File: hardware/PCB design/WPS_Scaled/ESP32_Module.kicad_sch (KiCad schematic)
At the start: 0 parts

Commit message: finalized the pcb schematics
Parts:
- added C20, C7: 100nF, symbol Device:C
- added C21, C23: 0.1uF, symbol Device:C
- added C22: 10uF, symbol Device:C_Polarized
- added C6: 22uF, symbol Device:C_Polarized
- added C8, C9: 1uF, symbol Device:C
- added D12, D13, D14, D4: LED, symbol Device:LED
- added D3: 1N5817-T, 1N5817-T:DIOAD1039W78L463D236, symbol COIL_1N5817-T:1N5817-T
- added R26, R27: 2.2k, symbol Device:R
- added R28, R5, R6: 10k, symbol Device:R
- added R3, R4: 5.1k, symbol Device:R
- added R7: 1k, symbol Device:R
- added S1, S2: SW_Push, symbol Switch:SW_Push
- added TP_BOOT1, TP_EN1, TP_RXD0, TP_SCL1, TP_SDA1, TP_TXD0: TestPoint, symbol Connector:TestPoint
- added U3: ESP32-S3-WROOM-1(N16R8), :WIRELM-SMD_ESP32-S3-WROOM-1, symbol COIL:ESP32-S3-WROOM-1(N16R8)
- added U4: TYPEC-306DDW-ARP16, :USB-C-TH_TYPEC-306DDW-ARP16, symbol COIL:TYPEC-306DDW-ARP16
- added U5: CH340C, :SOP-16_L10.0-W3.9-P1.27-LS6.0-BL, symbol COIL:CH340C
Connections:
- new net: D3.2, U4.16 (VBUS), U4.21 (VBUS), U4.4 (VBUS), U4.9 (VBUS)
- new net: D12.2 (A), R26.2
- new net: R3.2, U4.8 (CC1)
- new net: C21.1, U5.4 (V3)
- new net: D4.2 (A), R7.2
- new net: D14.2 (A), R28.2
- new net: R4.1, U4.20 (CC2)
- new net: D13.2 (A), R27.2
- new net: C22.2, C23.2, U5.16 (VCC)
- new net +12V: R28.1
- new net +3.3V: C6.1, C7.1, R5.1, R6.1, R7.1, U3.2 (3V3)
- new net +5V: C22.1, C23.1, D3.1, R26.1
- new net +5V_SW: R27.1
- new net ACTUATOR_PUMP_EN: U3.8 (IO15)
- new net ACTUATOR_UV_EN: U3.9 (IO16)
- new net ACTUATOR_VALVE_EN: U3.10 (IO17)
- new net BUTTON_BOOT: C9.2, R6.2, S2.2, TP_BOOT1.1, U3.27 (IO0)
- new net BUTTON_EN: C20.1, C8.2, R5.2, S1.2, TP_EN1.1, U3.3 (EN)
- new net BUTTON_SYSTEM_RESET: U3.23 (IO21)
- new net DISPLAY_SCL: U3.22 (IO14)
- new net DISPLAY_SDA: U3.21 (IO13)
- new net GND: C20.2, C21.2, C6.2, C7.2, C8.1, C9.1, D12.1 (K), D13.1 (K), D14.1 (K), D4.1 (K), R3.1, R4.2, S1.1, S2.1, U3.1 (GND), U3.40 (GND), U3.41 (GND), U4.1 (GND), U4.12 (GND), U4.13 (GND), U4.17 (SBU2), U4.18 (DN2), U4.19 (DP2), U4.20 (CC2), U4.24 (GND), U5.1 (GND)
- new net LED_MAINTENANCE: U3.12 (IO8)
- new net LED_POWER_ON: U3.11 (IO18)
- new net SENSOR_COLOR_SCL: TP_SCL1.1, U3.24 (IO47)
- new net SENSOR_COLOR_SDA: TP_SDA1.1, U3.25 (IO48)
- new net SENSOR_FLOW_SIGNAL: U3.39 (IO1)
- new net SENSOR_LEVEL_ECHO: U3.35 (IO42)
- new net SENSOR_LEVEL_TRIG: U3.38 (IO2)
- new net SENSOR_PH_SIGNAL: U3.5 (IO5)
- new net SENSOR_PRESSURE_SIGNAL: U3.7 (IO7)
- new net SENSOR_TDS_SIGNAL: U3.6 (IO6)
- new net SENSOR_TURBIDITY_SIGNAL: U3.4 (IO4)
- new net SWITCHED_5V_EN: U3.18 (IO10)
- new net UART_RX: TP_TXD0.1, U3.37 (TXD0), U5.3 (RXD)
- new net UART_TX: TP_RXD0.1, U3.36 (RXD0), U5.2 (TXD)
- new net USB_D+: U4.19 (DP2), U4.7 (DP1), U5.5 (D+)
- new net USB_D-: U4.18 (DN2), U4.6 (DN1), U5.6 (D-)
- no-connect marks 0 -> 26
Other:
- note added: "Caution: Limit total USB current draw to <500mA. Excessive peripheral (sensor) load may trigger host port overcurrent protection, requiring a system restart to reset the port."
- note added: "D4 - Led used to show 3.3V is supplied D12- Led used to show 5V is supplied D13 - Led used to show 5V_SW (required by sensors) is supplied D14 - Led used to show 12V is supplied"
- note added: "EN and BOOT Buttons"
- note added: "ESP32-S3-WROOM-1 module"
- note added: "Power Status Indicators"
- note added: "USB (TYPE-C) module"
- company: (none) -> Makerere University

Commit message: finallized pcb layout
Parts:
- added R30, R31, R32, R33: 4.7k, COIL:RES-TH_BD2.4-L6.3-P10.30-D0.6, symbol Device:R
- C20, C21, C23, C7: footprint (none) -> COIL:CAP-TH_L3.6-W2.3-P2.50-D0.5
- C22: footprint (none) -> COIL:CAP-TH_BD4.0-P2.50-D0.6-FD
- C6: footprint (none) -> COIL:CAP-TH_BD4.8-P2.54-D0.5-RD
- C8, C9: footprint (none) -> COIL:CAP-TH_L4.4-W4.0-P5.08-D0.6
- D3: footprint 1N5817-T:DIOAD1039W78L463D236 -> COIL:DO-27_BD5.2-L8.9-P12.90-D1.5-RD
- LED1: renamed from D4; footprint (none) -> COIL:LED-TH_BD5.9-P2.54-RD_RED
- LED2: renamed from D12; footprint (none) -> COIL:LED-TH_BD5.9-P2.54-RD_RED
- LED3: renamed from D13; footprint (none) -> COIL:LED-TH_BD5.9-P2.54-RD_RED
- LED4: renamed from D14; footprint (none) -> COIL:LED-TH_BD5.9-P2.54-RD_RED
- R26, R27, R28, R3, R4, R5, R6, R7: footprint (none) -> COIL:RES-TH_BD2.4-L6.3-P10.30-D0.6
- S1, S2: footprint (none) -> COIL:KEY-SMD_4P-L6.0-W6.0-P3.90-LS9.0
- TP10: renamed from TP_SDA1; value TestPoint -> SDA1; footprint (none) -> TestPoint:TestPoint_THTPad_D2.0mm_Drill1.0mm
- TP11: renamed from TP_SCL1; value TestPoint -> SCL1; footprint (none) -> TestPoint:TestPoint_THTPad_D2.0mm_Drill1.0mm
- TP6: renamed from TP_EN1; value TestPoint -> EN; footprint (none) -> TestPoint:TestPoint_THTPad_D2.0mm_Drill1.0mm
- TP7: renamed from TP_TXD0; value TestPoint -> TXD0; footprint (none) -> TestPoint:TestPoint_THTPad_D2.0mm_Drill1.0mm
- TP8: renamed from TP_RXD0; value TestPoint -> RXD0; footprint (none) -> TestPoint:TestPoint_THTPad_D2.0mm_Drill1.0mm
- TP9: renamed from TP_BOOT1; value TestPoint -> BOOT; footprint (none) -> TestPoint:TestPoint_THTPad_D2.0mm_Drill1.0mm
- U3: footprint :WIRELM-SMD_ESP32-S3-WROOM-1 -> COIL:WIRELM-SMD_ESP32-S3-WROOM-1
- U4: footprint :USB-C-TH_TYPEC-306DDW-ARP16 -> COIL:USB-C-TH_TYPEC-306DDW-ARP16
- U5: footprint :SOP-16_L10.0-W3.9-P1.27-LS6.0-BL -> COIL:SOP-16_L10.0-W3.9-P1.27-LS6.0-BL
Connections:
- net BUTTON_BOOT: now also C9.1, S2.1; no longer C9.2, S2.2
- net BUTTON_EN: now also C8.1, S1.1; no longer C8.2, S1.2
- net DISPLAY_SCL: now also R31.1
- net DISPLAY_SDA: now also R30.1
- net GND: now also C8.2, C9.2, S1.2, S2.2, U4.A1 (GND), U4.A12 (GND), U4.B1 (GND), U4.B12 (GND); no longer C8.1, C9.1, S1.1, S2.1, U4.1 (GND), U4.12 (GND), U4.13 (GND), U4.24 (GND)
- net SENSOR_COLOR_SCL: now also R33.2
- net SENSOR_COLOR_SDA: now also R32.1
- net LED2_P: now reaches LED2.2 (A), R26.2
- net USB_CC1: now reaches R3.2
- net USB_CC1: now also U4.A5 (CC1); no longer U4.8 (CC1)
- net USB_TO_UART_V3: now reaches C21.1, U5.4 (V3)
- net LED1_P: now reaches LED1.2 (A), R7.2
- net LED4_P: now reaches LED4.2 (A), R28.2
- net USB_CC2: now reaches R4.1
- net USB_CC2: now also U4.B5 (CC2); no longer U4.20 (CC2)
- net LED3_P: now reaches LED3.2 (A), R27.2
- net USB_TO_UART_VCC: now reaches C22.2, C23.2, U5.16 (VCC)
- net +12V renamed VBAT
- net +3.3V renamed +3V3
- net +3V3: now also R30.2, R31.2, R32.2, R33.1
- removed net USB_D+: U4.19 (DP2), U4.7 (DP1), U5.5 (D+)
- removed net USB_D-: U4.18 (DN2), U4.6 (DN1), U5.6 (D-)
- new net USB_DN: U4.A7 (DN1), U4.B7 (DN2), U5.6 (D-)
- new net USB_DP: U4.A6 (DP1), U4.B6 (DP2), U5.5 (D+)
- new net USB_VBUS: D3.2, U4.A4 (VBUS), U4.A9 (VBUS), U4.B4 (VBUS), U4.B9 (VBUS)
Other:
- note added: "Review: It is recommended to connect a 499 Ω series resistor to the U0TXD line to suppress harmonics.(TX line) Make power taces as thick as possible: Main 3.3V line ≥ 25 mil RF power pins (pin2 & pin3) ≥ 20 mil Other small power branches ≥ 10 mil"
- moved on the sheet: C20, C22, C23, C6, C7, C8, C9, LED1, LED2, LED3, LED4, R26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

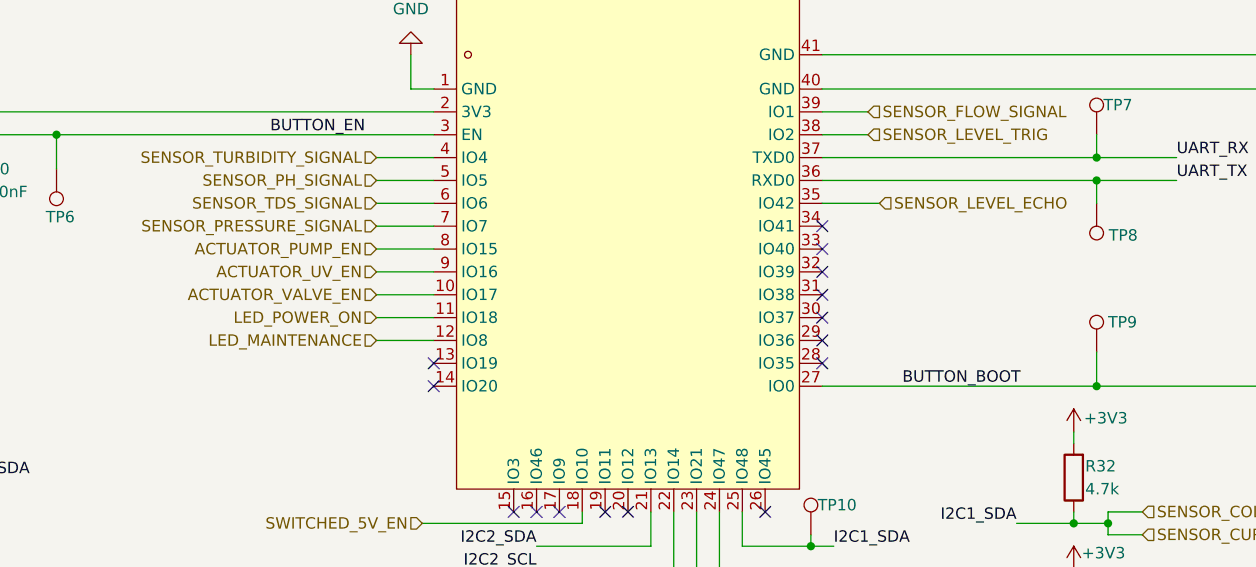
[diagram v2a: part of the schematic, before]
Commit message: started routing with sensors and critical signals
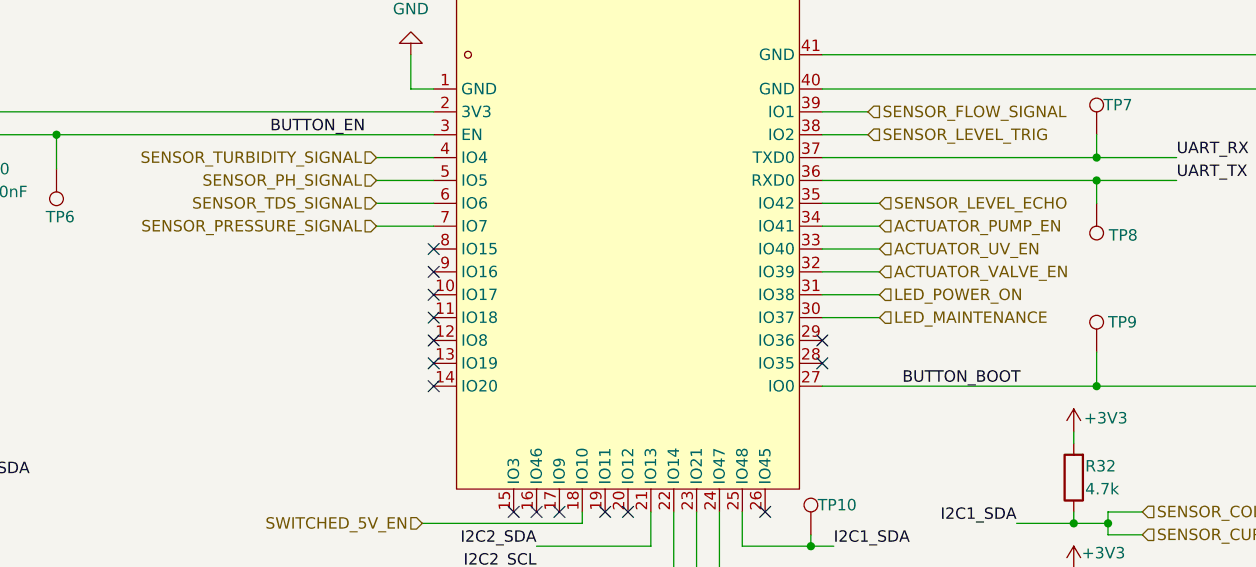
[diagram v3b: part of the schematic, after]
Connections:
- net ACTUATOR_PUMP_EN: now also U3.34 (IO41); no longer U3.8 (IO15)
- net ACTUATOR_UV_EN: now also U3.33 (IO40); no longer U3.9 (IO16)
- net ACTUATOR_VALVE_EN: now also U3.32 (IO39); no longer U3.10 (IO17)
- net LED_MAINTENANCE: now also U3.30 (IO37); no longer U3.12 (IO8)
- net LED_POWER_ON: now also U3.31 (IO38); no longer U3.11 (IO18)
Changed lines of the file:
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@@
-	)
-	(no_connect
-		(at 144.78 67.31)
-	)
-	(no_connect
-		(at 144.78 59.69)
 	)
 	(no_connect
@@
 	)
 	(no_connect
-		(at 144.78 62.23)
+		(at 101.6 69.85)
 	)
 	(no_connect
@@
 	)
 	(no_connect
+		(at 101.6 64.77)
+	)
+	(no_connect
 		(at 138.43 91.44)
 	)
@@
 	)
 	(no_connect
-		(at 144.78 69.85)
-	)
-	(no_connect
 		(at 44.45 157.48)
 	)
@@
 	)
 	(no_connect
+		(at 101.6 72.39)
+	)
+	(no_connect
 		(at 144.78 151.13)
 	)
 	(no_connect
+		(at 101.6 62.23)
+	)
+	(no_connect
 		(at 144.78 74.93)
 	)
@@
 	)
 	(no_connect
-		(at 144.78 64.77)
+		(at 101.6 67.31)
 	)
 	(wire
@@
 	(wire
 		(pts
+			(xy 144.78 69.85) (xy 151.13 69.85)
+		)
+		(stroke
+			(width 0)
+			(type default)
+		)
+	)
+	(wire
+		(pts
 			(xy 71.12 186.69) (xy 71.12 175.26)
 		)
@@
 	(wire
 		(pts
-			(xy 95.25 67.31) (xy 101.6 67.31)
-		)
-		(stroke
-			(width 0)
-			(type default)
-		)
-	)
-	(wire
-		(pts
 			(xy 115.57 151.13) (xy 121.92 151.13)
 		)
@@
 	(wire
 		(pts
-			(xy 95.25 72.39) (xy 101.6 72.39)
-		)
-		(stroke
-			(width 0)
-			(type default)
-		)
-	)
-	(wire
-		(pts
 			(xy 96.52 138.43) (xy 96.52 139.7)
 		)
@@
 	(wire
 		(pts
-			(xy 95.25 69.85) (xy 101.6 69.85)
-		)
-		(stroke
-			(width 0)
-			(type default)
-		)
-	)
-	(wire
-		(pts
 			(xy 57.15 134.62) (xy 22.86 134.62)
 		)
@@
 	(wire
 		(pts
+			(xy 144.78 59.69) (xy 151.13 59.69)
+		)
+		(stroke
+			(width 0)
+			(type default)
+		)
+	)
+	(wire
+		(pts
 			(xy 54.61 138.43) (xy 59.69 138.43)
 		)
@@
 	(wire
 		(pts
-			(xy 95.25 62.23) (xy 101.6 62.23)
-		)
-		(stroke
-			(width 0)
-			(type default)
-		)
-	)
-	(wire
-		(pts
 			(xy 135.89 95.25) (xy 143.51 95.25)
 		)
@@
 	(wire
 		(pts
+			(xy 144.78 67.31) (xy 151.13 67.31)
+		)
+		(stroke
+			(width 0)
+			(type default)
+		)
+	)
+	(wire
+		(pts
 			(xy 35.56 46.99) (xy 101.6 46.99)
 		)
@@
 	(wire
 		(pts
-			(xy 95.25 64.77) (xy 101.6 64.77)
-		)
-		(stroke
-			(width 0)
-			(type default)
-		)
-	)
-	(wire
-		(pts
 			(xy 257.81 66.04) (xy 261.62 66.04)
 		)
@@
 	(wire
 		(pts
+			(xy 144.78 64.77) (xy 151.13 64.77)
+		)
+		(stroke
+			(width 0)
+			(type default)
+		)
+	)
+	(wire
+		(pts
 			(xy 91.44 167.64) (xy 91.44 154.94)
 		)
@@
 		(pts
 			(xy 77.47 146.05) (xy 77.47 138.43)
+		)
+		(stroke
+			(width 0)
+			(type default)
+		)
+	)
+	(wire
+		(pts
+			(xy 144.78 62.23) (xy 151.13 62.23)
 		)
 		(stroke
@@
 	(hierarchical_label "ACTUATOR_UV_EN"
 		(shape input)
-		(at 95.25 64.77 180)
-		(effects
-			(font
-				(size 1.27 1.27)
-			)
-			(justify right)
+		(at 151.13 62.23 0)
+		(effects
+			(font
+				(size 1.27 1.27)
+			)
+			(justify left)
 		)
 	)
@@
 	(hierarchical_label "ACTUATOR_PUMP_EN"
 		(shape input)
-		(at 95.25 62.23 180)
-		(effects
-			(font
-				(size 1.27 1.27)
-			)
-			(justify right)
+		(at 151.13 59.69 0)
+		(effects
+			(font
+				(size 1.27 1.27)
+			)
+			(justify left)
 		)
 	)
@@
 	(hierarchical_label "ACTUATOR_VALVE_EN"
 		(shape input)
-		(at 95.25 67.31 180)
-		(effects
-			(font
-				(size 1.27 1.27)
-			)
-			(justify right)
+		(at 151.13 64.77 0)
+		(effects
+			(font
+				(size 1.27 1.27)
+			)
+			(justify left)
 		)
 	)
@@
 	(hierarchical_label "LED_POWER_ON"
 		(shape input)
-		(at 95.25 69.85 180)
-		(effects
-			(font
-				(size 1.27 1.27)
-			)
-			(justify right)
+		(at 151.13 67.31 0)
+		(effects
+			(font
+				(size 1.27 1.27)
+			)
+			(justify left)
 		)
 	)
@@
 	(hierarchical_label "LED_MAINTENANCE"
 		(shape input)
-		(at 95.25 72.39 180)
-		(effects
-			(font
-				(size 1.27 1.27)
-			)
-			(justify right)
-		)
-	)
+		(at 151.13 69.85 0)
+		(effects
+			(font
+				(size 1.27 1.27)
+			)
+			(justify left)
+		)
+	)
